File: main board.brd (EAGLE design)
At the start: 35 x 50 mm, 60 parts, among them SW1 BOOT_SW, SW2 RST_SW, X1 MINI-USB, Y1 SMDRESONATOR

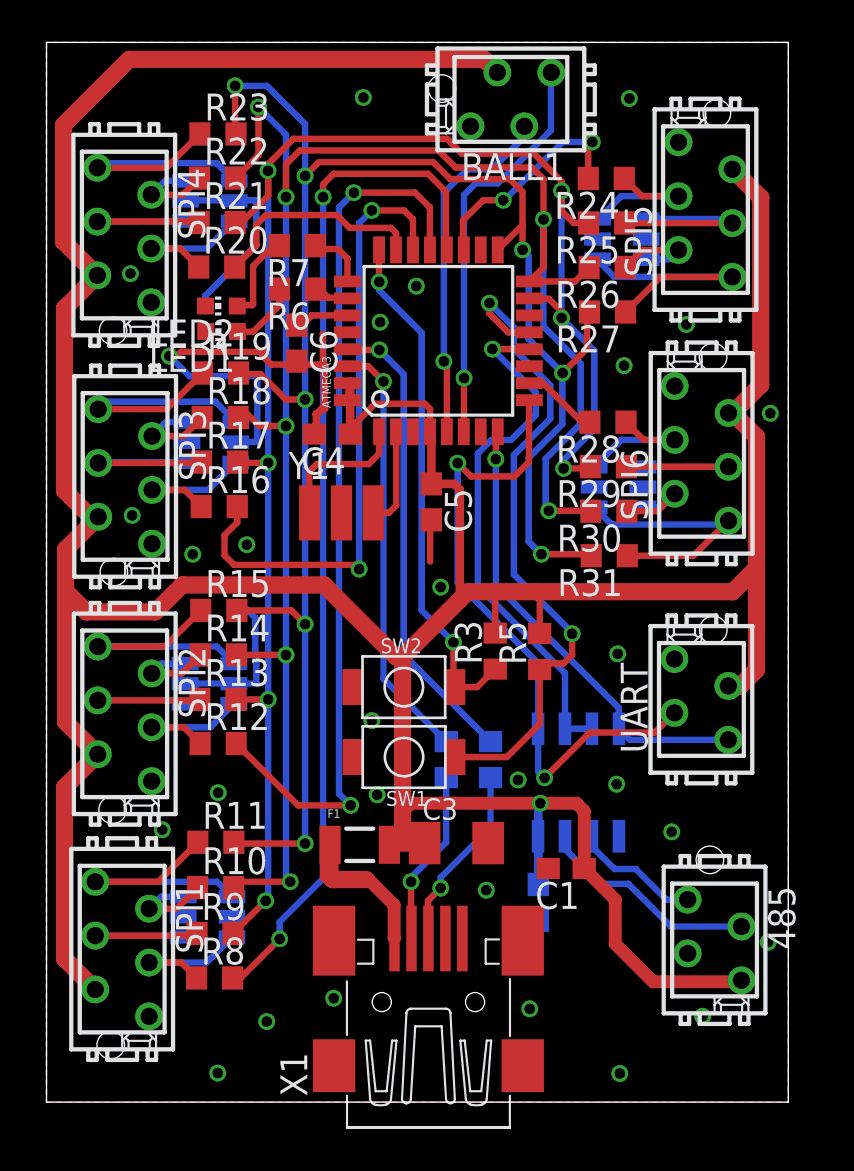
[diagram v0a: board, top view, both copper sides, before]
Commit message: All pins rooted into micromatches.
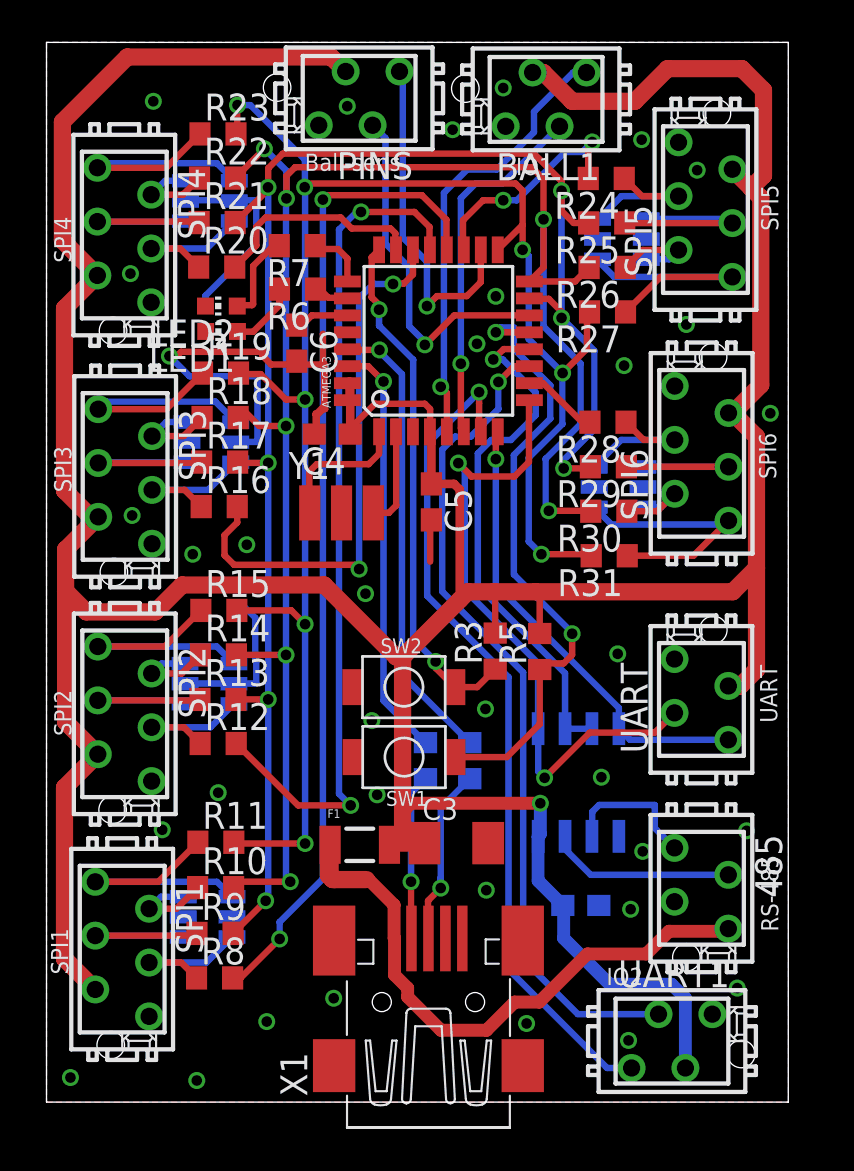
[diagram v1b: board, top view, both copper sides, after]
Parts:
- removed C1: 100nF, rcl:C0603
- added PINS, UART1: MICROMATCH-4, con-amp-micromatch:MICROMATCH-4
- moved 485 2.52 mm to (30.9, 10.1)
- moved C2 2.01 mm to (25.2, 9.28), turned to 180 degrees
- moved BALL1 1.66 mm to (23.6, 47.3)
- moved R1 0.98 mm to (17.9, 16.1)
- moved R2 0.98 mm to (20.0, 16.1)
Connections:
- removed net N$4: F1.1, X1.1
- new net B21: ATMEGA3.14, PINS.3
- new net B22: ATMEGA3.18, PINS.4
- new net B31: ATMEGA3.7, UART1.4
- new net B32: ATMEGA3.11, UART1.3
- new net PREFUSE: 485.1, F1.1, X1.1
- net B11: now also BALL1.4; no longer BALL1.3
- net B12: now also BALL1.3; no longer BALL1.4
- net GND: now also PINS.1, UART1.1; no longer C1.2
- net VCC: now also PINS.2, UART1.2; no longer 485.1, C1.1
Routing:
- net B32: track 0.00 -> 39.6 mm, vias 0 -> 1
- net B31: track 0.00 -> 39.5 mm, vias 0 -> 1
- net PREFUSE: track 0.00 -> 29.2 mm
- net B21: track 0.00 -> 16.9 mm, vias 0 -> 1
- net B22: track 0.00 -> 16.1 mm, vias 0 -> 1
- net N$4: track 8.41 -> 0.00 mm
- net VCC: track 193.0 -> 198.7 mm
- net MOSI: track 88.9 -> 84.1 mm
- net B11: track 16.7 -> 21.1 mm
- net SPI3: track 30.2 -> 26.5 mm
- net MISO: track 89.3 -> 86.4 mm
- net B12: track 19.3 -> 17.1 mm
- net SPI1: track 48.5 -> 46.6 mm
- net SPI2: track 42.1 -> 40.2 mm
- net N$7: track 31.5 -> 29.6 mm
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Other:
- board text added: "Ball-sens"
- board text added: "IO1"
- board text added: "IO2"
- board text added: "RS-485"
- board text added: "SPI1"
- board text added: "SPI2"
- board text added: "SPI3"
- board text added: "SPI4"
- board text added: "SPI5"
- board text added: "SPI6"
- board text added: "UART"

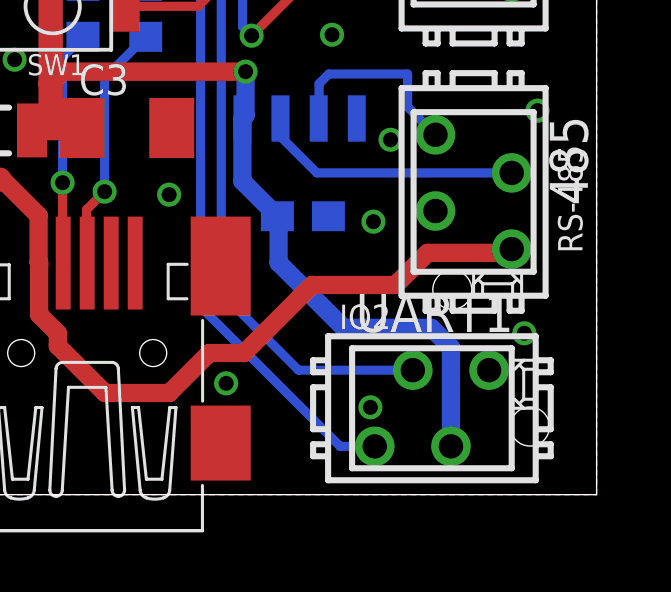
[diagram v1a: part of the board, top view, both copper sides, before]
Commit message: Rotated one micromatch.
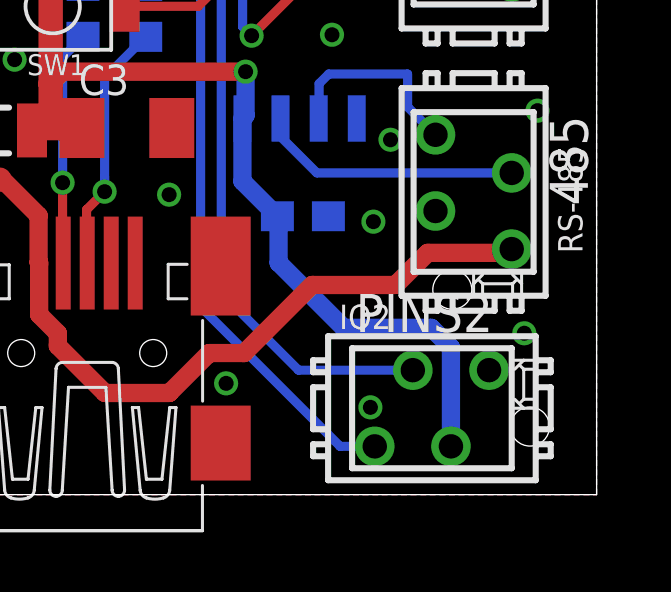
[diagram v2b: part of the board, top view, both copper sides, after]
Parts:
- renumbered UART1 to PINS2
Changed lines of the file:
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@@
 <attribute name="OC_FARNELL" value="3784629" x="30.9" y="10.09" size="1.778" layer="27" rot="R270" display="off"/>
 </element>
-<element name="UART1" library="con-amp-micromatch" package="MICROMATCH-4" value="MICROMATCH-4" x="29.51" y="2.88">
+<element name="PINS2" library="con-amp-micromatch" package="MICROMATCH-4" value="MICROMATCH-4" x="29.51" y="2.88">
 <attribute name="OC_NEWARK" value="19R8124" x="29.51" y="2.88" size="1.778" layer="27" display="off"/>
 <attribute name="MPN" value="7-215464-4" x="29.51" y="2.88" size="1.778" layer="27" display="off"/>
@@
 <via x="19.16" y="45.88" extent="1-16" drill="0.5"/>
 <via x="5.04" y="47.22" extent="1-16" drill="0.5"/>
-<contactref element="UART1" pad="1"/>
+<contactref element="PINS2" pad="1"/>
 <via x="20.31" y="35.78" extent="1-16" drill="0.5"/>
 <via x="15.05" y="23.99" extent="1-16" drill="0.5"/>
@@
 <wire x1="0.75" y1="46.25" x2="0.75" y2="40.655" width="0.8128" layer="1"/>
 <wire x1="0.75" y1="40.655" x2="2.4" y2="39.005" width="0.8128" layer="1"/>
-<contactref element="UART1" pad="2"/>
+<contactref element="PINS2" pad="2"/>
 <wire x1="30.145" y1="1.61" x2="30.145" y2="4.905" width="0.6096" layer="16"/>
 <wire x1="30.145" y1="4.905" x2="29.49" y2="5.56" width="0.6096" layer="16"/>
@@
 <wire x1="18.67" y1="24.09" x2="22.49" y2="20.27" width="0.3048" layer="16"/>
 <wire x1="22.49" y1="20.27" x2="22.49" y2="6.725" width="0.3048" layer="16"/>
-<contactref element="UART1" pad="3"/>
+<contactref element="PINS2" pad="3"/>
 <wire x1="22.49" y1="6.725" x2="25.065" y2="4.15" width="0.3048" layer="16"/>
 <wire x1="25.065" y1="4.15" x2="28.875" y2="4.15" width="0.3048" layer="16"/>
@@
 <wire x1="21.8" y1="20.05" x2="21.8" y2="6.26" width="0.3048" layer="16"/>
 <wire x1="21.8" y1="6.26" x2="26.45" y2="1.61" width="0.3048" layer="16"/>
-<contactref element="UART1" pad="4"/>
+<contactref element="PINS2" pad="4"/>
 <wire x1="26.45" y1="1.61" x2="27.605" y2="1.61" width="0.3048" layer="16"/>
 <wire x1="17.96" y1="23.89" x2="17.96" y2="31.05" width="0.3048" layer="16"/>

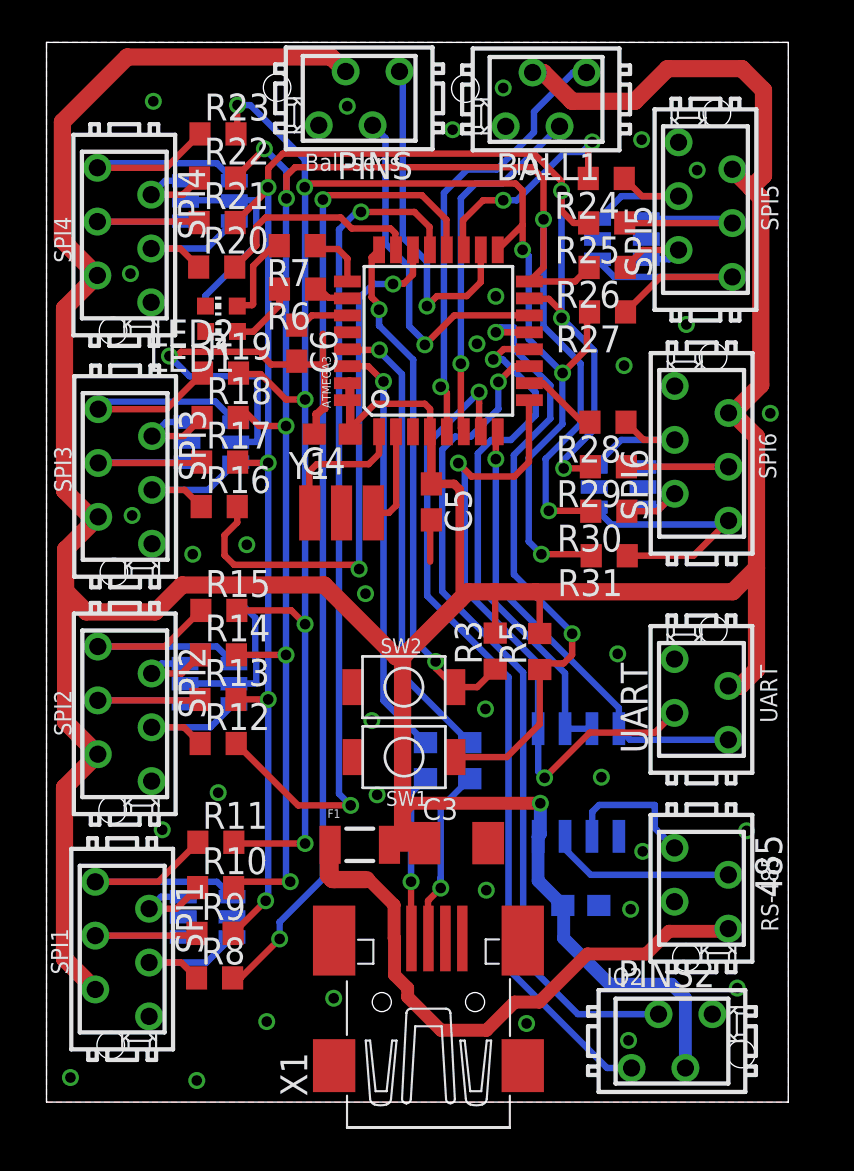
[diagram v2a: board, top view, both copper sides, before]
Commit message: Tweaks to GND plane
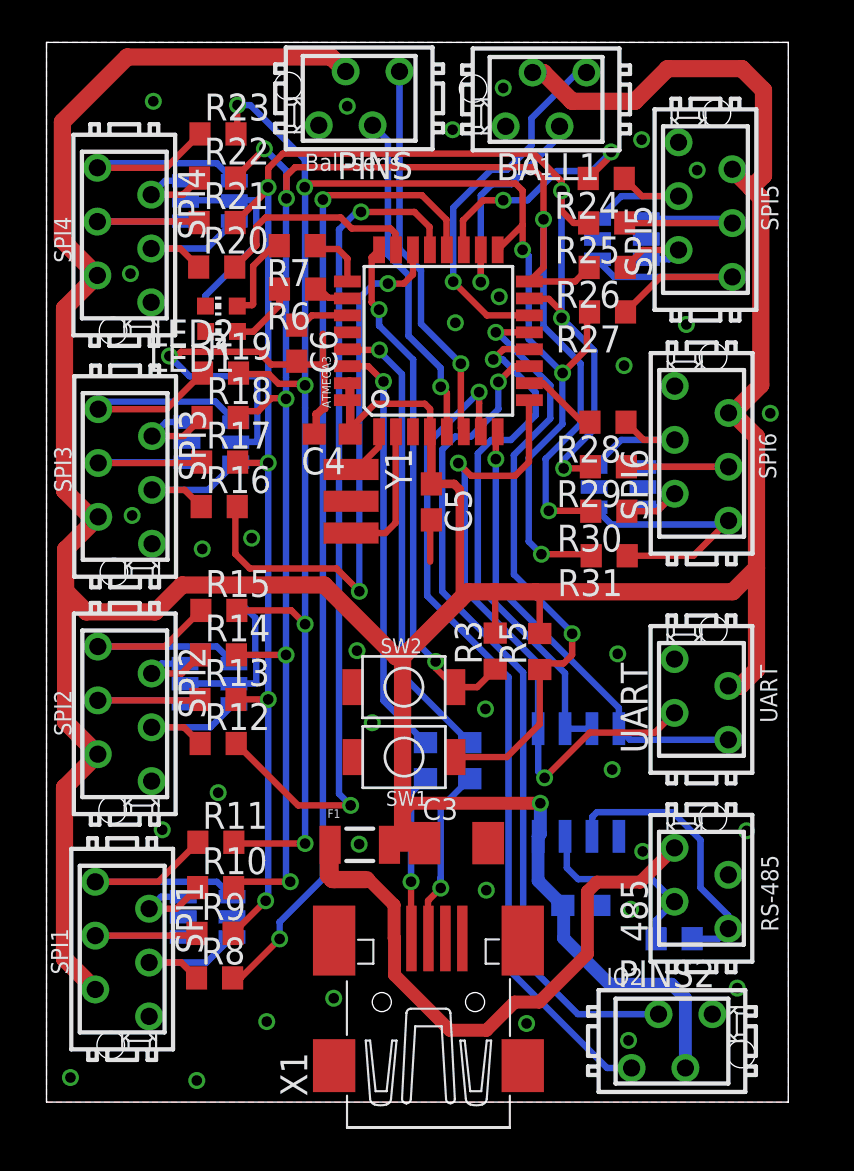
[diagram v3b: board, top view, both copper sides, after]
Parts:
- added R4: 120, rcl:R0603
- moved Y1 0.71 mm to (14.4, 28.4), turned to 270 degrees
- turned 485 to 90 degrees
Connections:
- net A: now also R4.2
- net B: now also R4.1
- net B11: now also PINS.3; no longer BALL1.4
- net B12: now also PINS.4; no longer BALL1.3
- net B21: now also BALL1.4; no longer PINS.3
- net B22: now also BALL1.3; no longer PINS.4
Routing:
- net A: track 7.13 -> 13.8 mm
- net B22: track 16.1 -> 11.0 mm
- net B11: track 21.1 -> 15.9 mm
- net N$5: track 6.63 -> 2.46 mm
- net N$6: track 4.71 -> 6.60 mm
- net B12: track 17.1 -> 18.3 mm
- net B: track 8.81 -> 9.98 mm
- net N$7: track 29.6 -> 28.8 mm
- net SPI5: track 10.8 -> 11.4 mm
- net B21: track 16.9 -> 17.4 mm
- net PREFUSE: track 29.2 -> 29.7 mm

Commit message: Also added some caps for button or whatever ports.
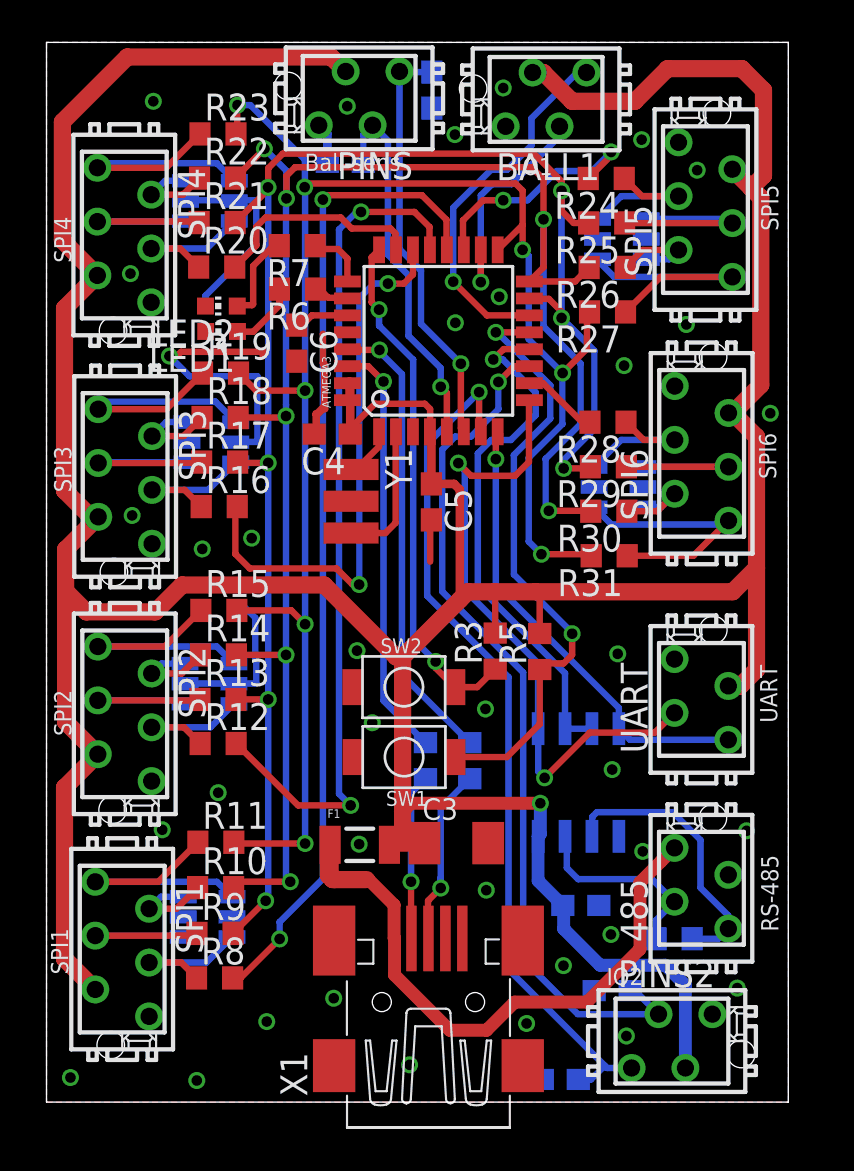
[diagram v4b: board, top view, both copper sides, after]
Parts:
- added C1, C7, C8, C9: 100nF, rcl:C0603
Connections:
- net B11: now also C7.1
- net B12: now also C1.1
- net B31: now also C8.1
- net B32: now also C9.1
- net GND: now also C1.2, C7.2, C8.2, C9.2
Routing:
- net B11: track 15.9 -> 17.8 mm
- net B32: track 39.6 -> 41.4 mm
- net B12: track 18.3 -> 19.9 mm
- net B31: track 39.5 -> 41.0 mm
- net GND: track 43.7 -> 42.6 mm, vias 35 -> 37
